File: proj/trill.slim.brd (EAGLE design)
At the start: 44.2 x 108.7 mm, 127 parts, among them J1 SPKRAST_01532MR, J2 MICCMA-4544PF-W, J3 ADAFRUIT_OLED_13, J4 DM3D-SFDM, J5 SJ1-3523N, J6 CONUFL001, M1 Z3OC_VIB_MOTOR, U1 SIM5300EA, U10 3.3V 600mA, U11 MCP1642B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

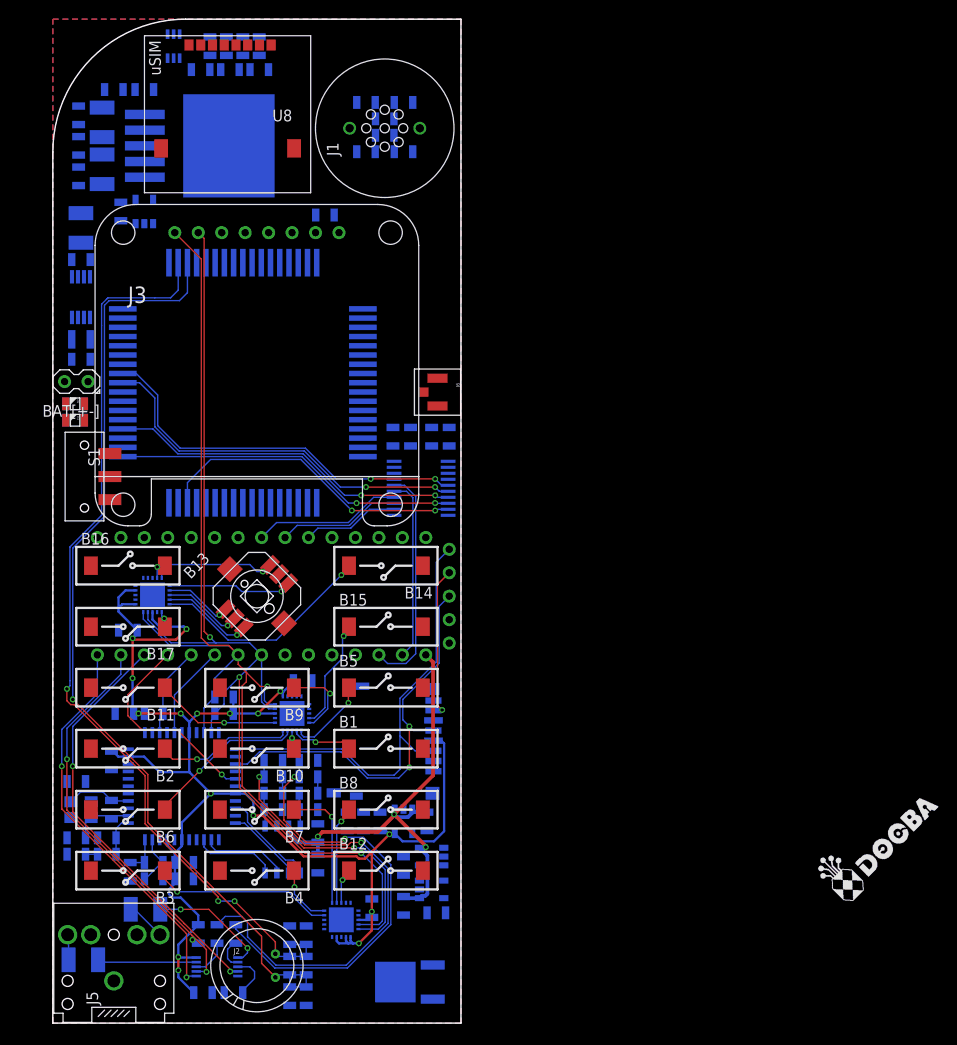
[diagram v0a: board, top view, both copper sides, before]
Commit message: Fixed SIM5300EA footprint in library (was missing restrict layer) Completed routing "slim" version of Trill mobile phone - so much awesome.
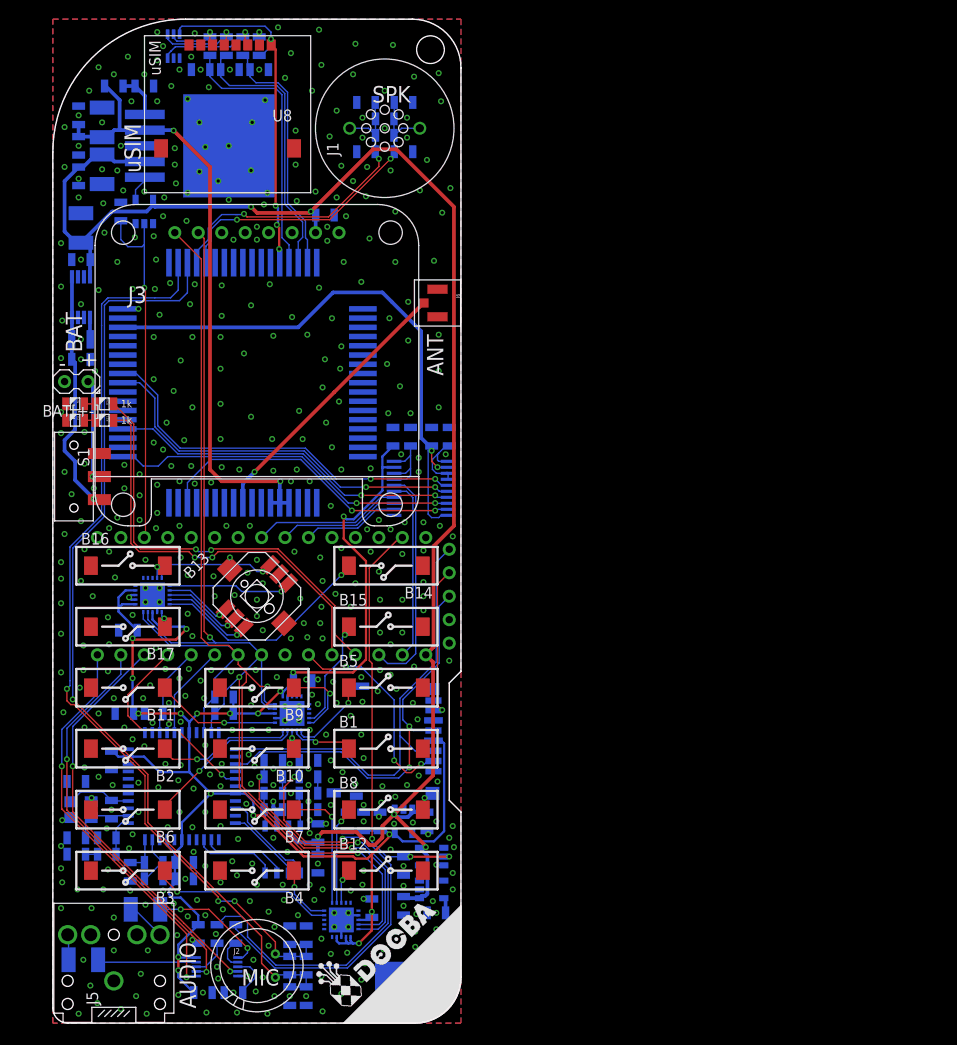
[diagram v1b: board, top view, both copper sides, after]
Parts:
- moved J6 9.65 mm to (41.7, 78.0)
- moved R21 3.18 mm to (5.59, 65.3), flipped to the top, turned to 180 degrees
- moved R24 3.18 mm to (5.59, 67.1), flipped to the top, turned to 180 degrees
- moved C2 1.91 mm to (36.8, 63.5)
- moved R1 1.91 mm to (38.7, 63.5)
- moved S1 1.14 mm to (2.29, 59.2)
- moved R4 0.38 mm to (9.91, 101.5)
- moved R5 0.38 mm to (6.60, 101.5)
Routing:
- net 5.0V: track 53.8 -> 179.1 mm, vias 3 -> 5
- net 3.8V: track 0.00 -> 68.3 mm, vias 0 -> 2
- net N$22: track 0.00 -> 62.2 mm, vias 0 -> 2
- net N$65: track 0.00 -> 47.0 mm, vias 0 -> 2
- net N$66: track 0.00 -> 45.2 mm, vias 0 -> 2
- net VIBRATOR_EN: track 0.00 -> 44.4 mm, vias 0 -> 3
- net GSM_PWR_EN: track 0.00 -> 39.1 mm, vias 0 -> 1
- net N$31: track 0.00 -> 39.0 mm, vias 0 -> 4
- net 3.3V: track 172.4 -> 210.4 mm, vias 16 -> 18
- net N$44: track 0.00 -> 36.0 mm, vias 0 -> 2
- net N$43: track 0.00 -> 35.8 mm, vias 0 -> 2
- net N$61: track 0.00 -> 29.8 mm, vias 0 -> 1
- net N$38: track 0.00 -> 29.7 mm
- net N$39: track 0.00 -> 29.4 mm
- net N$37: track 0.00 -> 27.0 mm
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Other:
- outline, holes or cut-outs redrawn
- board text added: "+"
- board text added: "-"
- board text added: "100k"
- board text added: "100nF"
- board text added: "100uF"
- board text added: "10k"
- board text added: "10pF"
- board text added: "10uF"
- board text added: "1k"
- board text added: "1uF"
- board text added: "2.7V"
- board text added: "22pF"
- board text added: "270k"
- board text added: "27pF"
- board text added: "3.3V"
- board text added: "3.3nF"
- board text added: "3.3uF"
- board text added: "33pF"
- board text added: "4.7R"
- board text added: "4.7nF"
- board text added: "4.7uH"
- board text added: "470R"
- board text added: "470pF"
- board text added: "47k"
- board text added: "51R"
- board text added: "560R"
- board text added: "74125"
- board text added: "ANT"
- board text added: "AUDIO"
- board text added: "BAT"
- board text added: "CS4334"
- board text added: "ESDA"
- board text added: "LM4811"
- board text added: "MCP1642B"
- board text added: "MCP23008"
- board text added: "MIC"
- board text added: "MIC29302"
- board text added: "MicroSD"
- board text added: "SIM5300EA"
- board text added: "SPK"
- board text added: "STA013"
- board text added: "TXB0108"
- board text added: "VIBRATION MOTOR"
- board text added: "ioNode"
- board text added: "uSIM"
